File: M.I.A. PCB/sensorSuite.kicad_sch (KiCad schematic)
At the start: 21 parts, among them J2 Conn_Coaxial, U3 MMC5983MA, U4 ICM-45686, U5 MS5611-01BA, U6 TMP117xxDRV, U7 MAX-M10S, U8 KX134-1211

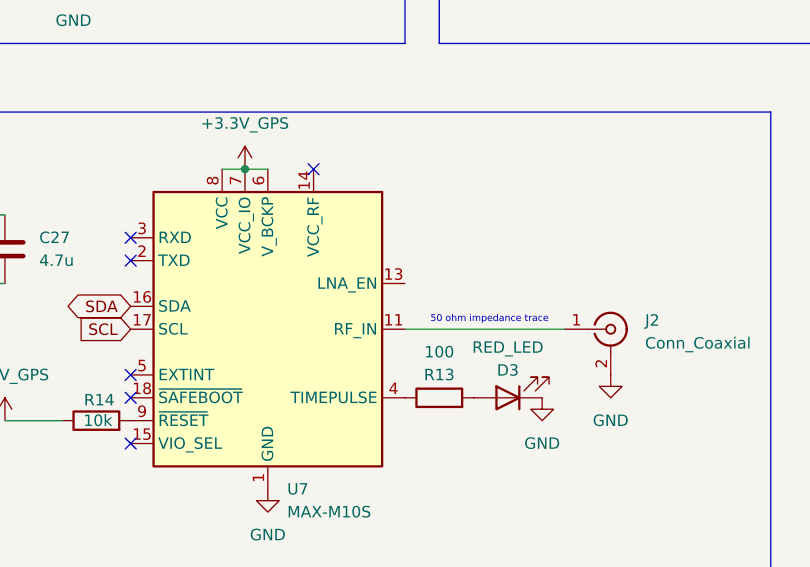
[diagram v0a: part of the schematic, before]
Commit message: Added Test Points + Back Graphics
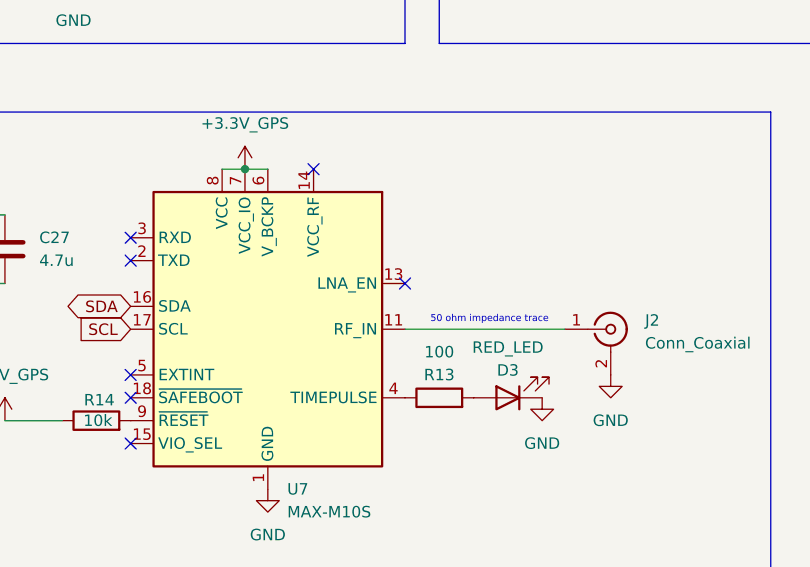
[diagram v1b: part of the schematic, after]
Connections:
- no-connect marks 14 -> 15
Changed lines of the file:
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@@
+	)
+	(no_connect
+		(at 90.17 147.32)
 	)
 	(no_connect
